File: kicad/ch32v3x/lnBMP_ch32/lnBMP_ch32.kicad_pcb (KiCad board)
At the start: 2 copper layers, 72.6 x 33 mm, 24 parts, among them J1 BMP Debug1, J2 BMP Debug2, J3 Debug port, J4 USB_OTG, SW1 SW_DIP_x01, SW2 SW_DIP_x01, U1 CH32V303RCT6, U2 LM1117-3.3, Y1 Crystal

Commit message: kicad: minor update
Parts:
- moved J4 8.11 mm to (154.7, 92.6)
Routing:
- net GND: track 236.4 -> 226.7 mm
- net Net-(J4-VBUS): track 38.0 -> 28.6 mm
- net D-: track 26.0 -> 21.7 mm
- net D+: track 25.6 -> 21.6 mm
- net unconnected-(U1-PC11-Pad52): track 2.46 -> 2.75 mm, vias 0 -> 1
- net UART TX: track 7.11 -> 7.28 mm, vias 0 -> 1
- added copper zone on B.Cu, net GND
- added copper zone on F.Cu, net GND
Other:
- board size 72.6 x 33 mm -> 56 x 33 mm

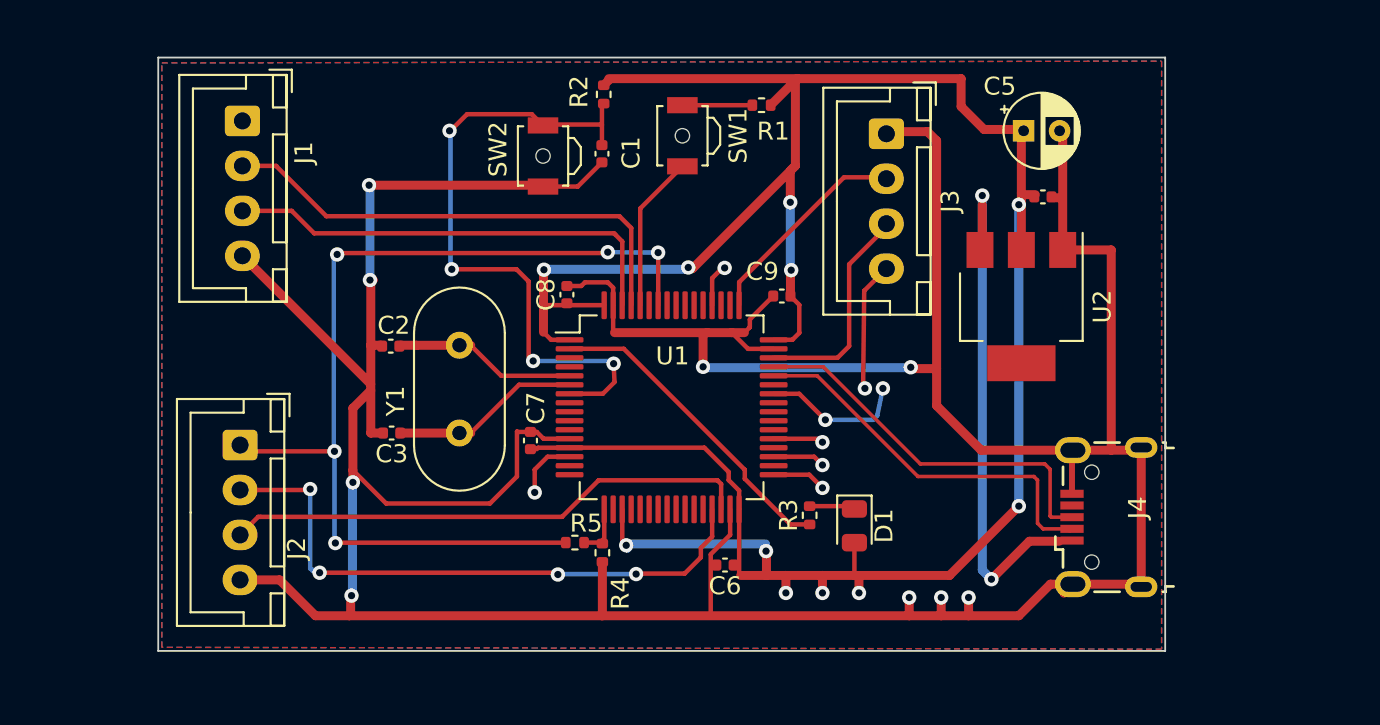
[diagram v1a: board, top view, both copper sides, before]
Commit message: update CH32 PCB to rev B
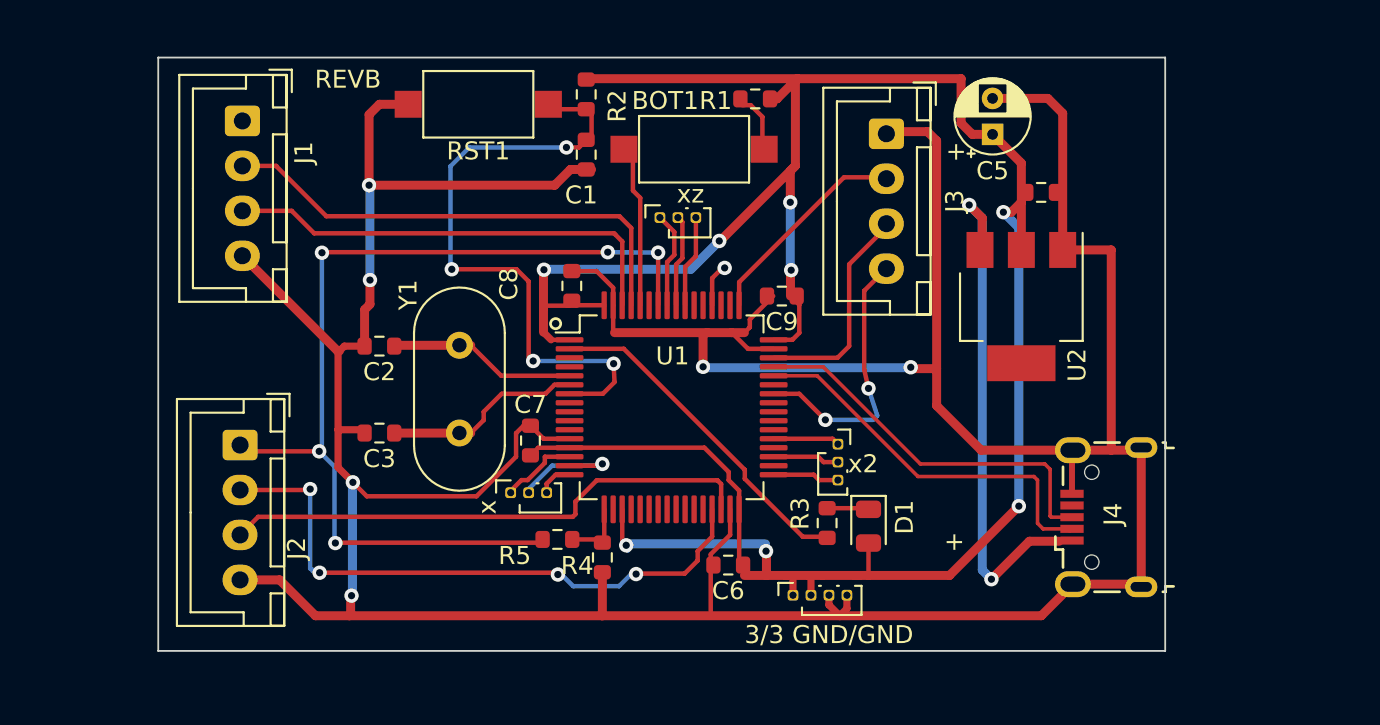
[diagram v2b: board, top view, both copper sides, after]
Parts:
- added 3/3 GND/GND: PinSocket_1x04_P1.00mm_Vertical, Connector_PinSocket_1.00mm:PinSocket_1x04_P1.00mm_Vertical, F.Cu at (137.3, 96.9)
- added x: PinSocket_1x03_P1.00mm_Vertical, Connector_PinSocket_1.00mm:PinSocket_1x03_P1.00mm_Vertical, F.Cu at (121.6, 91.2)
- added x2: PinSocket_1x03_P1.00mm_Vertical, Connector_PinSocket_1.00mm:PinSocket_1x03_P1.00mm_Vertical, F.Cu at (139.8, 88.5)
- added xz: PinSocket_1x03_P1.00mm_Vertical, Connector_PinSocket_1.00mm:PinSocket_1x03_P1.00mm_Vertical, F.Cu at (129.9, 75.9)
- BOT1: renamed from SW1; footprint Button_Switch_SMD:SW_SPST_B3U-3000P-B -> Button_Switch_SMD:SW_SPST_CK_RS282G05A3
- C1, C2, C3, C5, C6, C7, C8, C9: footprint Capacitor_SMD:C_0402_1005Metric -> Resistor_SMD:R_0603_1608Metric
- R1, R2, R3, R4, R5: footprint Resistor_SMD:R_0402_1005Metric -> Resistor_SMD:R_0603_1608Metric
- RST1: renamed from SW2; footprint Button_Switch_SMD:SW_SPST_B3U-3000P-B -> Button_Switch_SMD:SW_SPST_CK_RS282G05A3
- moved RST1 4.61 mm to (119.8, 69.6), turned to 180 degrees
- moved C4 1.74 mm to (148.4, 71.3), turned to 90 degrees
- moved R3 1.06 mm to (139.2, 92.9)
- moved BOT1 0.99 mm to (131.8, 72.1), turned to 180 degrees
- moved R5 0.99 mm to (124.2, 93.8)
- moved R2 0.98 mm to (125.8, 69.0)
- moved C1 0.88 mm to (125.8, 72.4)
- moved D1 0.78 mm to (141.5, 93.1)
- moved C3 0.68 mm to (114.3, 87.9)
- moved C2 0.63 mm to (114.3, 83.0)
- moved C8 0.56 mm to (125.0, 79.7)
- moved R1 0.49 mm to (135.2, 69.3)
- moved C5 0.27 mm to (151.1, 74.5)
- moved R4 0.26 mm to (126.7, 94.8)
- moved C6 0.18 mm to (133.7, 95.2)
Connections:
- J3 pad 4: UART TX -> UART_TX
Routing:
- net UART TX: track 7.28 -> 0.00 mm, vias 1 -> 0
- net UART_TX: track 8.15 -> 15.2 mm
- net unconnected-(U1-PA1-Pad15): track 0.00 -> 6.26 mm, vias 0 -> 1
- net unconnected-(U1-PB5-Pad57): track 0.00 -> 5.37 mm
- net unconnected-(U1-PB4-Pad56): track 0.00 -> 5.12 mm
- net unconnected-(U1-PB3-Pad55): track 0.00 -> 5.12 mm
- net GND: track 226.7 -> 230.2 mm, vias 9 -> 6
- net unconnected-(U1-PA2-Pad16): track 0.00 -> 1.98 mm
- net Net-(U1-PC13): track 17.7 -> 19.0 mm
- net INOUT_NRESET: track 55.6 -> 54.6 mm
- net unconnected-(U1-PC6-Pad37): track 2.79 -> 3.70 mm, vias 1 -> 0
- net unconnected-(U1-PA0-Pad14): track 3.51 -> 4.36 mm, vias 1 -> 0
- net unconnected-(U1-PB14-Pad35): track 2.90 -> 3.70 mm, vias 1 -> 0
- net unconnected-(U1-PB12-Pad33): track 3.02 -> 3.70 mm, vias 1 -> 0
- net OUT_UART_TX: track 33.7 -> 34.3 mm
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- removed copper zone on B.Cu, net GND
- removed copper zone on F.Cu, net GND
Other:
- board text added: "+"
- board text added: "REVB"

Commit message: update ch32 pcba
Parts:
- added PA4567: PinSocket_1x04_P1.00mm_Vertical, Connector_PinSocket_1.00mm:PinSocket_1x04_P1.00mm_Vertical, F.Cu at (128.6, 96.5)
- 3/3/GND/GND: renamed from 3/3 GND/GND
- moved R2 5.21 mm to (123.9, 73.9), turned to 90 degrees
- moved C1 4.36 mm to (121.5, 73.1), turned to 180 degrees
- moved BOT1 3.08 mm to (130.0, 69.6)
- moved D1 2.58 mm to (143.9, 94.0), turned to 0 degrees
- moved x2 1.92 mm to (141.3, 89.7)
- moved R1 1.58 mm to (136.1, 70.6), turned to 90 degrees
- moved R3 1.40 mm to (139.9, 94.1), turned to 0 degrees
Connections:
- U1 pad 35: unconnected-(U1-PB14-Pad35) -> IN_FORCE_DFU
- x2 pad 2: unconnected-(U1-PB14-Pad35) -> IN_FORCE_DFU
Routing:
- net GND: track 230.2 -> 224.2 mm
- net IN_FORCE_DFU: track 0.00 -> 5.70 mm
- net +3.3V: track 142.7 -> 137.1 mm, vias 8 -> 9
- net unconnected-(U1-PA7-Pad23): track 0.00 -> 5.12 mm, vias 0 -> 1
- net unconnected-(U1-PA6-Pad22): track 0.00 -> 4.91 mm, vias 0 -> 1
- net unconnected-(U1-PA4-Pad20): track 0.00 -> 4.85 mm, vias 0 -> 1
- net unconnected-(U1-PA5-Pad21): track 0.00 -> 4.71 mm, vias 0 -> 1
- net unconnected-(U1-PB14-Pad35): track 3.70 -> 0.00 mm
- net Net-(U1-BOOT0): track 8.84 -> 12.3 mm
- net UART_TX: track 15.2 -> 12.6 mm
- net unconnected-(U1-PC6-Pad37): track 3.70 -> 5.70 mm
- net unconnected-(U1-PB12-Pad33): track 3.70 -> 5.70 mm
- net Net-(BOT1-Pad1): track 3.44 -> 2.27 mm

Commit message: update ch32 pcb
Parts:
- moved J4 2.68 mm to (152.1, 92.0)
- renumbered xz to PB567
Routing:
- net D-: track 21.7 -> 18.0 mm
- net D+: track 21.6 -> 17.9 mm
- net Net-(J4-VBUS): track 28.6 -> 25.8 mm
- net +3.3V: track 137.1 -> 136.4 mm
- net GND: track 224.2 -> 223.5 mm
- added copper zone on B.Cu, net GND
- added copper zone on F.Cu, net GND
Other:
- board size 56 x 33 mm -> 52.6 x 33 mm
- board text added: "GND"
- board text added: "RST"
- board text added: "RX"
- board text added: "SWDCLK"
- board text added: "SWDIO"
- board text added: "TX"
- board text added: "locked"

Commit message: kicad : Update ch32 and stm32 pcbs
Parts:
- R4, R5: value 1k -> 10k
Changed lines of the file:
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@@
-(kicad_pcb (version 20230410) (generator pcbnew)
+(kicad_pcb (version 20230517) (generator pcbnew)
   (general
     (thickness 1.6)
+    (legacy_teardrops)
   )
   (paper "A4")
@@
       (effects (font (size 1 1) (thickness 0.15)))
     )
-    (fp_text value "330" (at 0 1.43 360) (layer "F.Fab")
+    (fp_text value "330" (at 0 1.43) (layer "F.Fab")
       (effects (font (size 1 1) (thickness 0.15)))
     )
@@
     (fp_line (start 0.8 0.4125) (end -0.8 0.4125)
       (stroke (width 0.1) (type solid)) (layer "F.Fab"))
-    (fp_text user "${REFERENCE}" (at 0 0 360) (layer "F.Fab")
+    (fp_text user "${REFERENCE}" (at 0 0) (layer "F.Fab")
       (effects (font (size 0.4 0.4) (thickness 0.06)))
     )
@@
     (property "ki_keywords" "R resistor")
     (attr smd)
-    (fp_text reference "R1" (at 0.1 1.7 270) (layer "F.SilkS")
-      (effects (font (size 1 1) (thickness 0.15)))
-    )
-    (fp_text value "10k" (at 0 1.43 270) (layer "F.Fab")
+    (fp_text reference "R1" (at 0.1 1.7 -90) (layer "F.SilkS")
+      (effects (font (size 1 1) (thickness 0.15)))
+    )
+    (fp_text value "10k" (at 0 1.43 -90) (layer "F.Fab")
       (effects (font (size 1 1) (thickness 0.15)))
     )
@@
     (fp_line (start -0.8 0.4125) (end -0.8 -0.4125)
       (stroke (width 0.1) (type solid)) (layer "F.Fab"))
-    (fp_text user "${REFERENCE}" (at 0 0 270) (layer "F.Fab")
+    (fp_text user "${REFERENCE}" (at 0 0 -90) (layer "F.Fab")
       (effects (font (size 0.4 0.4) (thickness 0.06)))
     )
@@
       (effects (font (size 1 1) (thickness 0.15)))
     )
-    (fp_text value "100n" (at 0 1.43 180) (layer "F.Fab")
+    (fp_text value "100n" (at 0 1.43 -180) (layer "F.Fab")
       (effects (font (size 1 1) (thickness 0.15)))
     )
@@
     (fp_line (start -0.8 -0.4125) (end 0.8 -0.4125)
       (stroke (width 0.1) (type solid)) (layer "F.Fab"))
-    (fp_text user "${REFERENCE}" (at 0 0 180) (layer "F.Fab")
+    (fp_text user "${REFERENCE}" (at 0 0 -180) (layer "F.Fab")
       (effects (font (size 0.4 0.4) (thickness 0.06)))
     )
@@
     (property "ki_keywords" "LED diode")
     (attr smd)
-    (fp_text reference "D1" (at 1.9 -2 360) (layer "F.SilkS")
-      (effects (font (size 1 1) (thickness 0.15)))
-    )
-    (fp_text value "LED" (at 0 1.65 360) (layer "F.Fab")
+    (fp_text reference "D1" (at 1.9 -2) (layer "F.SilkS")
+      (effects (font (size 1 1) (thickness 0.15)))
+    )
+    (fp_text value "LED" (at 0 1.65) (layer "F.Fab")
       (effects (font (size 1 1) (thickness 0.15)))
     )
@@
     (fp_line (start 1 0.6) (end 1 -0.6)
       (stroke (width 0.1) (type solid)) (layer "F.Fab"))
-    (fp_text user "${REFERENCE}" (at 0 0 360) (layer "F.Fab")
+    (fp_text user "${REFERENCE}" (at 0 0) (layer "F.Fab")
       (effects (font (size 0.5 0.5) (thickness 0.08)))
     )
@@
       (effects (font (size 1 1) (thickness 0.15)))
     )
-    (fp_text value "1k" (at 0 1.43 90) (layer "F.Fab")
+    (fp_text value "10k" (at 0 1.43 90) (layer "F.Fab")
       (effects (font (size 1 1) (thickness 0.15)))
     )
@@
     (property "ki_keywords" "R resistor")
     (attr smd)
-    (fp_text reference "R2" (at 0 1.6 270) (layer "F.SilkS")
-      (effects (font (size 1 1) (thickness 0.15)))
-    )
-    (fp_text value "10k" (at 0 1.43 270) (layer "F.Fab")
+    (fp_text reference "R2" (at 0 1.6 -90) (layer "F.SilkS")
+      (effects (font (size 1 1) (thickness 0.15)))
+    )
+    (fp_text value "10k" (at 0 1.43 -90) (layer "F.Fab")
       (effects (font (size 1 1) (thickness 0.15)))
     )
@@
     (fp_line (start -0.8 0.4125) (end -0.8 -0.4125)
       (stroke (width 0.1) (type solid)) (layer "F.Fab"))
-    (fp_text user "${REFERENCE}" (at 0 0 270) (layer "F.Fab")
+    (fp_text user "${REFERENCE}" (at 0 0 -90) (layer "F.Fab")
       (effects (font (size 0.4 0.4) (thickness 0.06)))
     )
@@
       (effects (font (size 1 1) (thickness 0.15)))
     )
-    (fp_text value "1k" (at 0 1.43) (layer "F.Fab")
-      (effects (font (size 1 1) (thickness 0.15)))
-    )
+    (fp_text value "10k" (at 0 1.43) (layer "F.Fab")
+      (effects (font (size 1 1) (thickness 0.15)))
+    )
